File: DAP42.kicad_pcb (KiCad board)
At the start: 2 copper layers, 64 x 39 mm, 40 parts, among them J1 JTAG, J2 Target JTAG, J3 USB_B, Q1 AO3401, SW1 WKUP, U1 W25Q128FV, U2 STM32F042K6Tx, U3 LM1117-3.3, U4 USBLC6-2SC6, U5 USBLC6-2SC6, U6 USBLC6-2SC6, U7 USBLC6-2SC6, U8 USBLC6-2SC6, U9 USBLC6-2SC6, Y1 8MHz

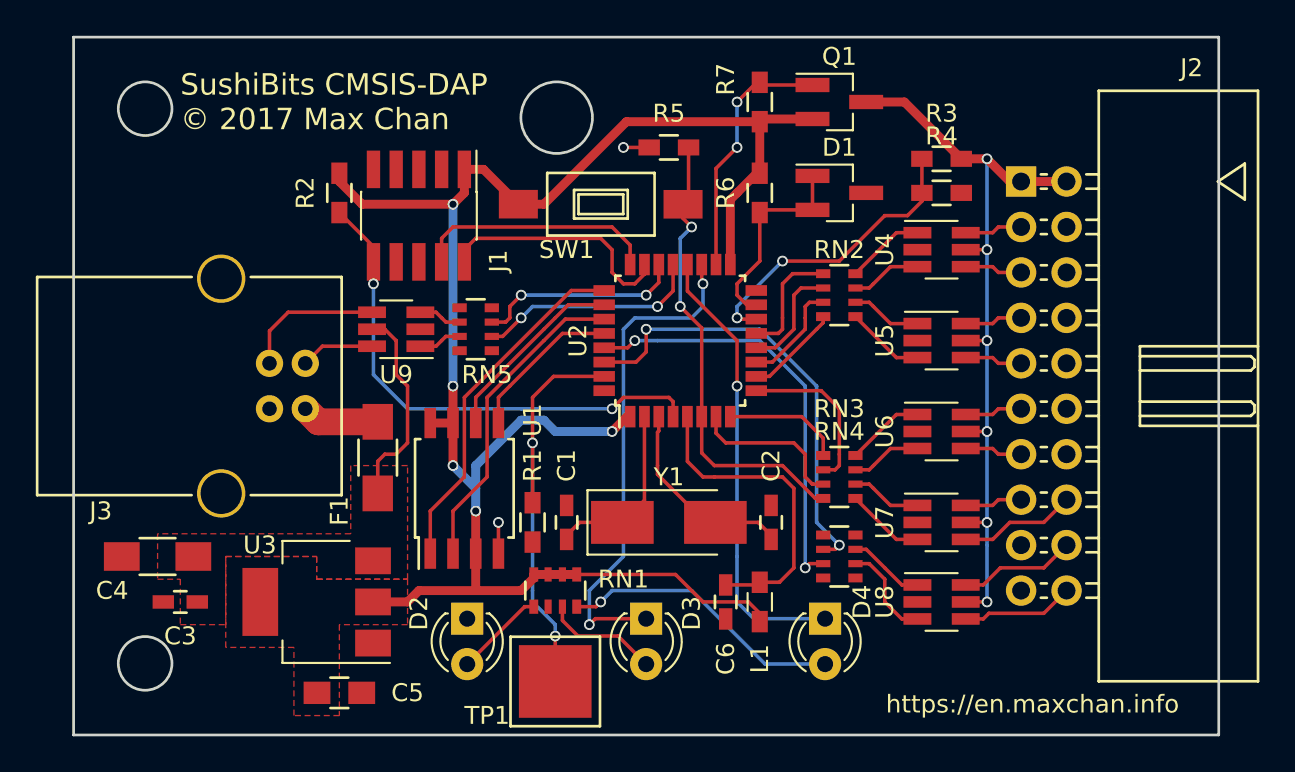
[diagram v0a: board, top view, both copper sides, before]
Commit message: Changing the power delivery subsystem.
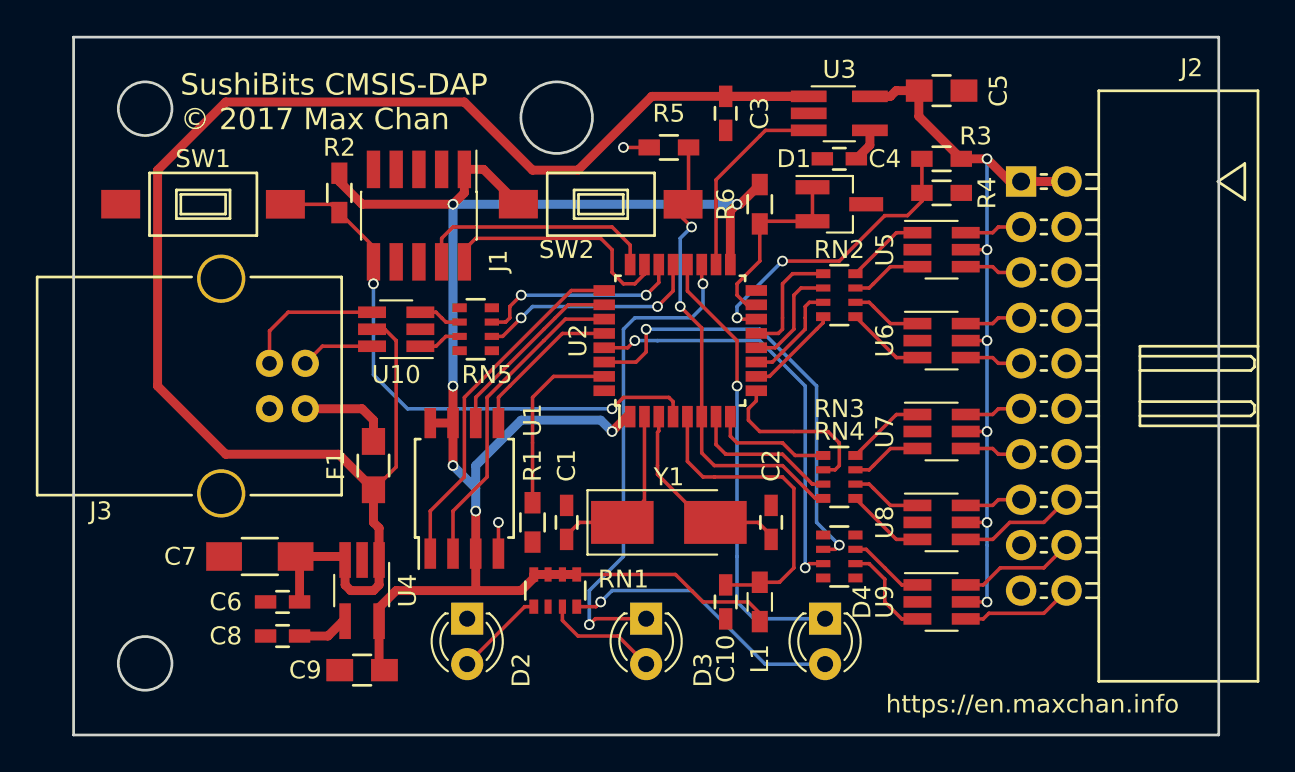
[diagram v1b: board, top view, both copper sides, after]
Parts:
- removed Q1: AO3401, TO_SOT_Packages_SMD:SOT-23_Handsoldering
- removed R7: 10k, Resistors_SMD:R_0603_HandSoldering
- removed TP1: BOOT0, SMD_Packages:1Pin
- added C3: 100n, Capacitors_SMD:C_0603_HandSoldering, F.Cu at (154.4, 84.8)
- added C4: 100n, Capacitors_SMD:C_0603_HandSoldering, F.Cu at (160.8, 87.3)
- added C5: 10µ, Capacitors_SMD:C_0805_HandSoldering, F.Cu at (166.5, 83.5)
- added C8: 100n, Capacitors_SMD:C_0603_HandSoldering, F.Cu at (129.7, 114.0)
- added SW1: RESET, Buttons_Switches_SMD:SW_SPST_FSMSM, F.Cu at (125.2, 89.8)
- added U4: LD3985G33R, TO_SOT_Packages_SMD:TSOT-23-5_HandSoldering, F.Cu at (134.1, 111.4)
- C9: renamed from C5; value 10u -> 10µ
- F1: value 1A -> 500mA; footprint Resistors_SMD:R_1206_HandSoldering -> Resistors_SMD:R_0805_HandSoldering
- U3: value LM1117-3.3 -> LD3985G33R; footprint TO_SOT_Packages_SMD:SOT-223 -> TO_SOT_Packages_SMD:TSOT-23-5_HandSoldering
- moved U3 40.0 mm to (160.8, 84.8), turned to 0 degrees
- moved C6 5.72 mm to (129.7, 112.1)
- moved C7 5.72 mm to (128.4, 109.5)
- moved C9 1.80 mm to (134.1, 115.9), turned to 180 degrees
- moved D1 0.64 mm to (160.8, 89.8)
- moved R6 0.64 mm to (156.3, 89.8)
- moved F1 0.51 mm to (134.8, 104.4)
- renumbered C6 to C10, C3 to C6, C4 to C7, SW1 to SW2, U9 to U10, U4 to U5, U5 to U6, U6 to U7, U7 to U8, U8 to U9
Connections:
- U3 pad 1: GND -> +5V
- U3 pad 2: VDD -> GND
- U3 pad 3: +5V -> /TGT_PEN
- U3 pad 4: VDD -> Net-(C4-Pad1)
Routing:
- net +5V: track 11.5 -> 97.8 mm
- net Net-(R1-Pad1): track 24.2 -> 10.4 mm, vias 2 -> 0
- net /TGT_PEN: track 14.3 -> 11.1 mm, vias 2 -> 0
- net /DBG_~RST: track 28.6 -> 31.8 mm
- net Net-(C8-Pad1): track 0.00 -> 2.89 mm
- net VDD: track 99.2 -> 96.8 mm, vias 5 -> 6
- net Net-(C4-Pad1): track 0.00 -> 1.90 mm
- net /TGT_VDD: track 43.8 -> 44.8 mm
- net Net-(F1-Pad2): track 4.35 -> 5.26 mm
- net /ADC_CAL: track 11.3 -> 10.7 mm
- removed copper zone on F.Cu, net +5V
- removed copper zone on F.Cu, net VDD
